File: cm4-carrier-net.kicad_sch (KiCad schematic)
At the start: 59 parts, among them J1 USB_C_Receptacle_USB2.0, J2 Micro_SD_Card, J3 Abracon_ARJM11-502, J5 block, Q1 DMP2066LSN, SW1 BOOT, SW2 GLOBAL_EN, SW3 USB_OTG, U1 TPS54302, U5 Compute_Module_4_Functional, U6 TPD2EUSB30

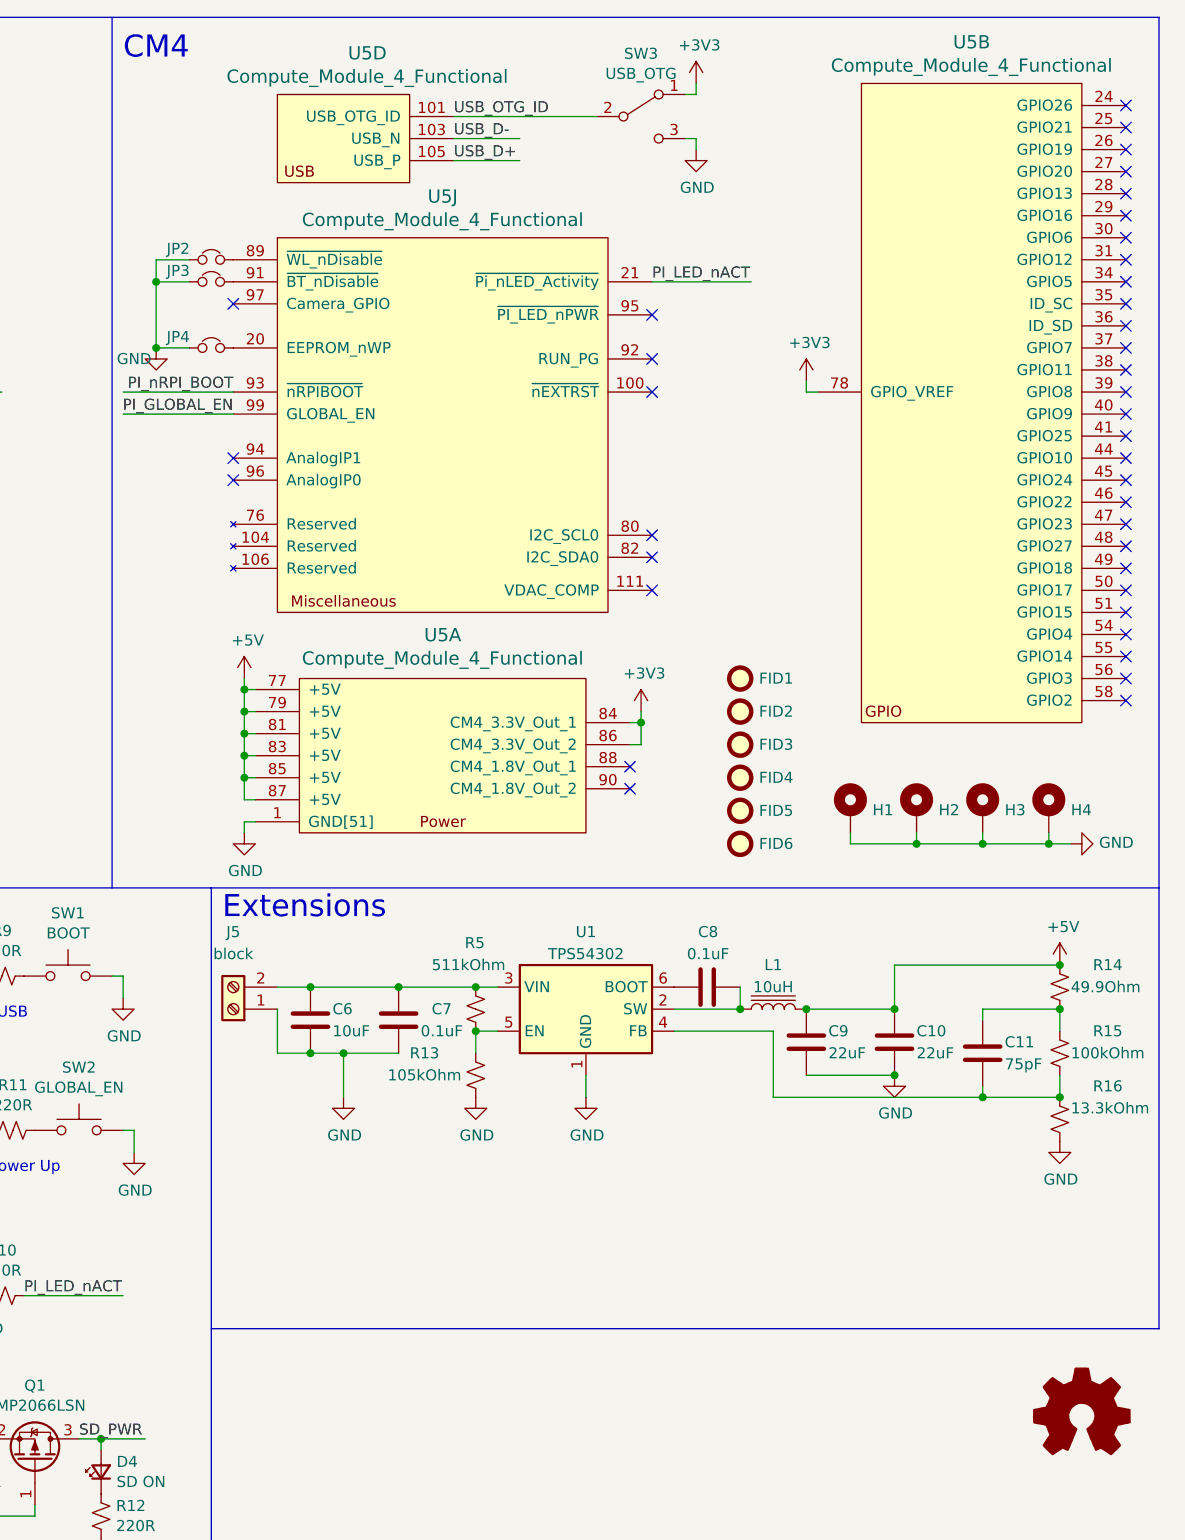
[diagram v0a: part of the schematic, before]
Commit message: added power protection and some layout changes
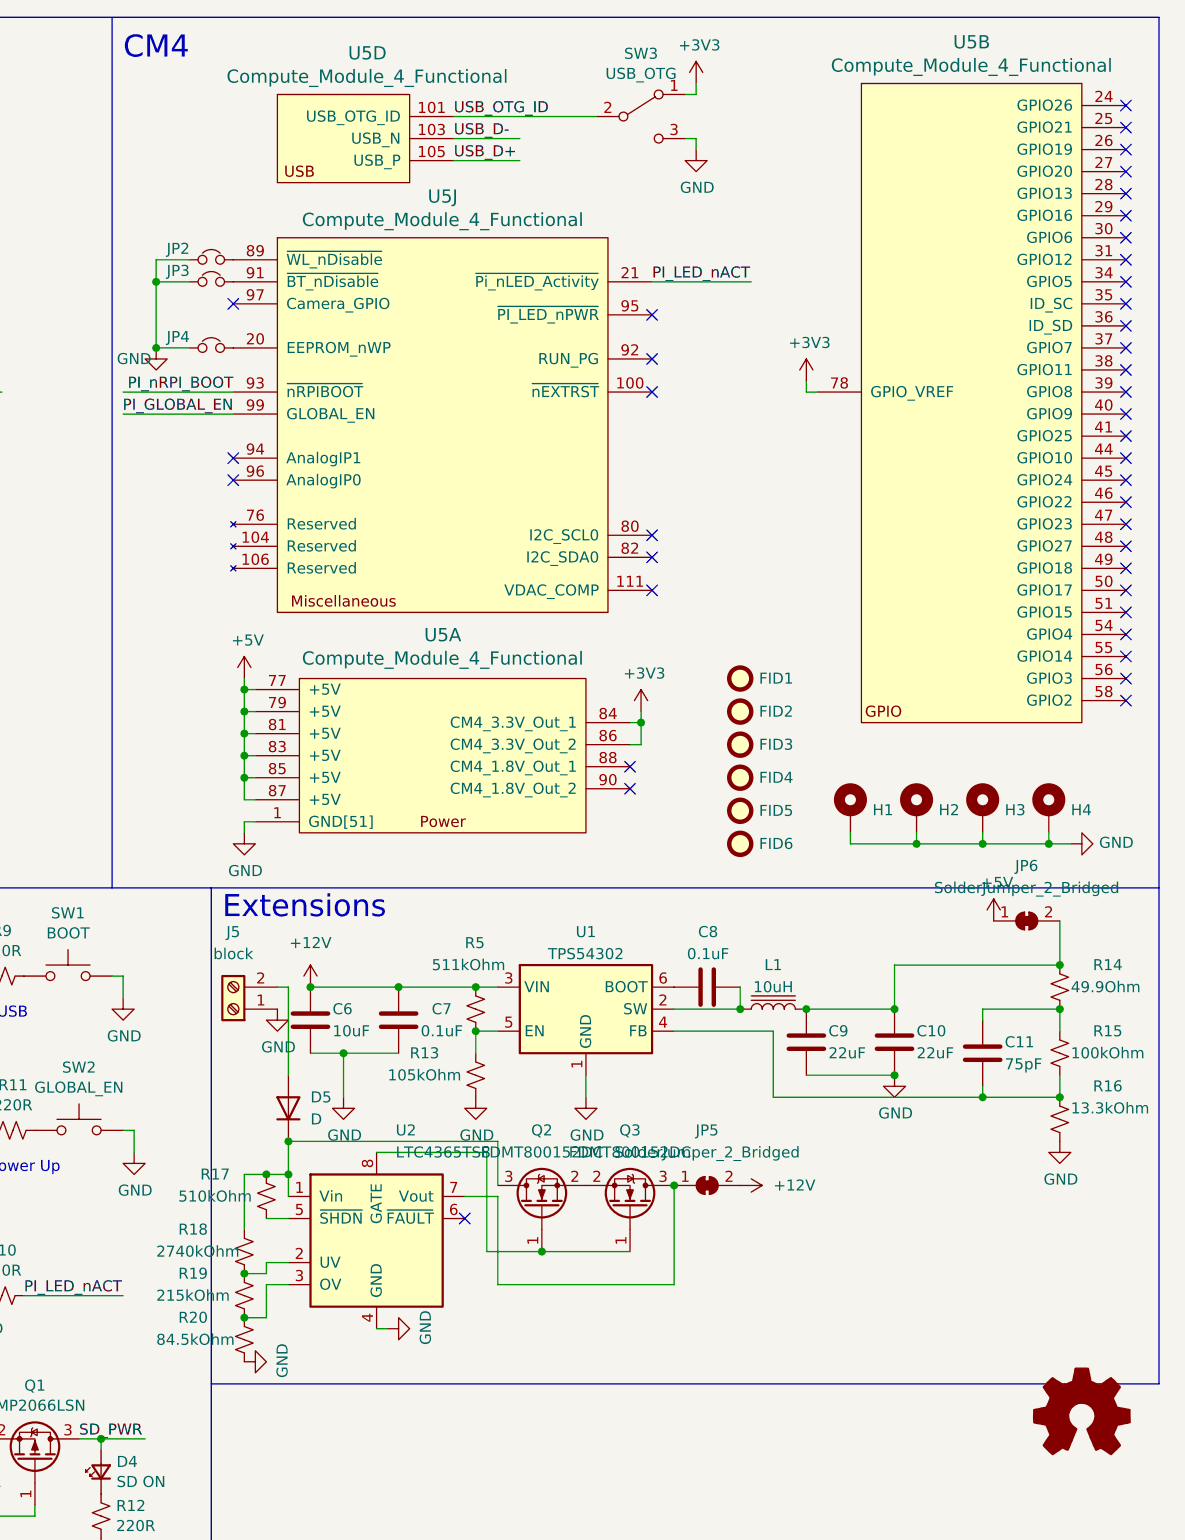
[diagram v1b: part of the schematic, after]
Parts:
- added D5: D, Diode_SMD:D_2010_5025Metric_Pad1.52x2.65mm_HandSolder, symbol Device:D
- added JP5, JP6: SolderJumper_2_Bridged, Jumper:SolderJumper-2_P1.3mm_Bridged2Bar_RoundedPad1.0x1.5mm, symbol Jumper:SolderJumper_2_Bridged
- added Q2, Q3: FDMT800152DC, Package_TO_SOT_SMD:PQFN_8x8, symbol Transistor_FET:FDMT800152DC
- added R17: 510kOhm, Resistor_SMD:R_0603_1608Metric, symbol Device:R_Small_US
- added R18: 2740kOhm, Resistor_SMD:R_0603_1608Metric, symbol Device:R_Small_US
- added R19: 215kOhm, Resistor_SMD:R_0603_1608Metric, symbol Device:R_Small_US
- added R20: 84.5kOhm, Resistor_SMD:R_0603_1608Metric, symbol Device:R_Small_US
- added U2: LTC4365TS8, Package_TO_SOT_SMD:TSOT-23-8, symbol Power_Management:LTC4365TS8
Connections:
- net +5V: now also JP6.1 (A); no longer C10.1, C9.1, L1.2, R14.1
- net GND: now also R20.2, U2.4 (GND)
- net +12V: now reaches C6.1, C7.1, R5.1, U1.3 (VIN)
- net +12V: now also JP5.2 (B); no longer J5.2 (Pin_2)
- new net: Q2.1 (G), Q3.1 (G), U2.8 (GATE)
- new net: Q2.2 (S), Q3.2 (S)
- new net: JP5.1 (A), Q3.3 (D), U2.7 (Vout)
- new net: D5.1 (K), Q2.3 (D), R17.1, R18.1, U2.1 (Vin)
- new net: R17.2, U2.5 (~{SHDN})
- new net: C10.1, C9.1, JP6.2 (B), L1.2, R14.1
- new net: R19.2, R20.1, U2.3 (OV)
- new net: D5.2 (A), J5.2 (Pin_2)
- new net: R18.2, R19.1, U2.2 (UV)
- no-connect marks 47 -> 48

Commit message: a couple of changes
fully removed cm4!
added orange pi cm4 footprint.
added extra usb 2 port.
removed unneeded diode.
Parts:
- removed D5: D, Diode_SMD:D_2010_5025Metric_Pad1.52x2.65mm_HandSolder, symbol Device:D
- removed JP1: eMMC, jkiv-library:J_Small_NC, symbol cm4-carrier-net-rescue:Jumper_NC_Small-Device
- removed JP2: ~WL_nDisable, jkiv-library:J_Small_NC, symbol cm4-carrier-net-rescue:Jumper_NC_Small-Device
- removed JP3: ~BT_nDisable, jkiv-library:J_Small_NC, symbol cm4-carrier-net-rescue:Jumper_NC_Small-Device
- removed JP4: EEPROM_nWP, jkiv-library:J_Small_NC, symbol cm4-carrier-net-rescue:Jumper_NC_Small-Device
- removed SW3: USB_OTG, Button_Switch_SMD:SW_SPDT_CK-JS102011SAQN, symbol Switch:SW_SPDT
- removed U5: Compute_Module_4_Functional, RPi_Compute_Module_4:Raspberry-Pi-4-Compute-Module, symbol cm4-carrier-net-rescue:Compute_Module_4_Functional-Raspberry_Pi_Compute_Module_4
- added J6: USB_A, Connector_USB:USB_A_Receptacle_GCT_USB1046, symbol Connector:USB_A
- added JP7: ~WL_nDisable, Jumper:SolderJumper-2_P1.3mm_Bridged2Bar_Pad1.0x1.5mm, symbol cm4-carrier-net-rescue:Jumper_NC_Small-Device
- added JP8: ~BT_nDisable, Jumper:SolderJumper-2_P1.3mm_Bridged2Bar_Pad1.0x1.5mm, symbol cm4-carrier-net-rescue:Jumper_NC_Small-Device
- added SW4: USB_OTG, Button_Switch_SMD:SW_SPDT_CK-JS102011SAQN, symbol Switch:SW_SPDT
- added U3: ORANGE_PI_CM4, Orange-Pi-CM4:MODULE_ORANGE_PI_CM4, symbol Orange-Pi-CM4:ORANGE_PI_CM4
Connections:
- net +3V3: no longer D2.2 (A), D3.2 (A), J3.13, Q1.2 (S), R8.2
- net +5V: now also C10.2, J6.1 (VBUS), U3.JP1_77 (VBUS_JP1_77), U3.JP1_79 (VBUS_JP1_79), U3.JP1_81 (VBUS_JP1_81), U3.JP1_83 (VBUS_JP1_83), U3.JP1_85 (VBUS_JP1_85), U3.JP1_87 (VBUS_JP1_87)
- net E0_LEDL: now also U3.JP1_15 (PHY0_LED2/CFG_LDO1)
- net E0_TR0+: now also U3.JP1_12 (PHY0_MDI_0+)
- net E0_TR0-: now also U3.JP1_10 (PHY0_MDI_0-)
- net E0_TR1+: now also U3.JP1_4 (PHY0_MDI_1+)
- net E0_TR1-: now also U3.JP1_6 (PHY0_MDI_1-)
- net E0_TR2+: now also U3.JP1_11 (PHY0_MDI_2+)
- net E0_TR2-: now also U3.JP1_9 (PHY0_MDI_2-)
- net E0_TR3+: now also U3.JP1_3 (PHY0_MDI_3+)
- net E0_TR3-: now also U3.JP1_5 (PHY0_MDI_3-)
- net GND: now also C10.1, J6.4 (GND), J6.5 (Shield), JP7.1, JP8.1, SW4.3 (C), U3.JP1_1 (GND_JP1_1), U3.JP1_13 (GND_JP1_13), U3.JP1_14 (GND_JP1_14), U3.JP1_2 (GND_JP1_2), U3.JP1_22 (GND_JP1_22), U3.JP1_23 (GND_JP1_23), U3.JP1_32 (GND_JP1_32), U3.JP1_33 (GND_JP1_33), U3.JP1_42 (GND_JP1_42), U3.JP1_43 (GND_JP1_43), U3.JP1_52 (GND_JP1_52), U3.JP1_53 (GND_JP1_53), U3.JP1_59 (GND_JP1_59), U3.JP1_60 (GND_JP1_60), U3.JP1_65 (GND_JP1_65), U3.JP1_66 (GND_JP1_66), U3.JP1_7 (GND_JP1_7), U3.JP1_71 (GND_JP1_71), U3.JP1_74 (GND_JP1_74), U3.JP1_8 (GND_JP1_8), U3.JP1_98 (GND_JP1_98), U3.JP2_13 (GND_JP2_13), U3.JP2_14 (GND_JP2_14), U3.JP2_19 (GND_JP2_19), U3.JP2_20 (GND_JP2_20), U3.JP2_25 (GND_JP2_25), U3.JP2_26 (GND_JP2_26), U3.JP2_31 (GND_JP2_31), U3.JP2_32 (GND_JP2_32), U3.JP2_37 (GND_JP2_37), U3.JP2_38 (GND_JP2_38), U3.JP2_44 (GND_JP2_44), U3.JP2_50 (GND_JP2_50), U3.JP2_55 (GND_JP2_55), U3.JP2_56 (GND_JP2_56), U3.JP2_61 (GND_JP2_61), U3.JP2_62 (GND_JP2_62), U3.JP2_67 (GND_JP2_67), U3.JP2_68 (GND_JP2_68), U3.JP2_7 (GND_JP2_7), U3.JP2_73 (GND_JP2_73), U3.JP2_74 (GND_JP2_74), U3.JP2_79 (GND_JP2_79), U3.JP2_8 (GND_JP2_8), U3.JP2_80 (GND_JP2_80), U3.JP2_85 (GND_JP2_85), U3.JP2_86 (GND_JP2_86), U3.JP2_91 (GND_JP2_91), U3.JP2_92 (GND_JP2_92), U3.JP2_97 (GND_JP2_97), U3.JP2_98 (GND_JP2_98), U3.JP3_1 (GND_JP3_1), U3.JP3_13 (GND_JP3_13), U3.JP3_14 (GND_JP3_14), U3.JP3_17 (GND_JP3_17), U3.JP3_2 (GND_JP3_2), U3.JP3_20 (GND_JP3_20), U3.JP3_23 (GND_JP3_23), U3.JP3_7 (GND_JP3_7); no longer C10.2
- net PI_GLOBAL_EN: now also U3.JP1_99 (PMIC_PWRON)
- net PI_LED_nACT: now also U3.JP1_21 (DIY_LED)
- net PI_nRPI_BOOT: now also U3.JP1_93 (BOOT-SW)
- net SD_CLK: now also U3.JP1_57 (SDMMC0_CLK)
- net SD_CMD: now also U3.JP1_62 (SDMMC0_CMD)
- net SD_D0: now also U3.JP1_63 (SDMMC0_D0)
- net SD_D1: now also U3.JP1_67 (SDMMC0_D1)
- net SD_D2: now also U3.JP1_69 (SDMMC0_D2)
- net SD_D3: now also U3.JP1_61 (SDMMC0_D3)
- net SD_PWR_ON: now also U3.JP1_75 (SD_PWR_ON)
- net USB_D+: now also U3.JP2_1 (USB_OTG0_ID)
- net USB_D-: now also U3.JP2_3 (USB_OTG0_DM)
- net USB_OTG_ID: now also SW4.2 (B), U3.JP2_5 (USB_OTG0_DP)
- net ~{E0_LEDL}: now also U3.JP1_17 (PHY0_LED1/CFG_LDO0)
- net ~{E0_LEDR}: now also U3.JP1_19 (PHY0_LED0/CFG_EXT)
- net at Q2.3 (D), R17.1, R18.1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: now also J5.2 (Pin_2)
- net at C9.1, JP6.2 (B), L1.2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: no longer C10.1
- new net: JP7.2, U3.JP1_89 (~{WL_DIS})
- new net: JP8.2, U3.JP1_91 (~{BT_DIS})
- new net +1V8: U3.JP1_88 (VCC_1V8_JP1_88), U3.JP1_90 (VCC_1V8_JP1_90)
- new net +3.3V: D2.2 (A), D3.2 (A), J3.13, Q1.2 (S), R8.2, SW4.1 (A), U3.JP1_78 (VCCIO6), U3.JP1_84 (VCC_3V3_JP1_84), U3.JP1_86 (VCC_3V3_JP1_86)
- new net USB+: J6.3 (D+), U3.JP3_11 (USB2_HOST2_DP)
- new net USB-: J6.2 (D-), U3.JP3_9 (USB2_HOST2_DM)
- no-connect marks 48 -> 3
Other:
- note added: "Just pretend that everything outside of the outline is in here ;)"
- note removed: "Short = use eMMC Open = use SD card"
- moved on the sheet: C10

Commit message: added a pin header for the daughter board
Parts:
- added J4: 20021121-00010C4LF, digikey-footprints:PinHeader_2x5_P1.27mm, symbol dk_Rectangular-Connectors-Headers-Male-Pins:20021121-00010C4LF
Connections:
- net +5V: now also J4.1, J4.2
- net GND: now also J4.10, J4.9
- net I2C1_SCL-: now reaches U3.JP1_80 (I2C1_SCL_M0)
- net I2C1_SCL-: now also J4.5
- net I2C1_SDA+: now reaches U3.JP1_82 (I2C1_SDA_M0)
- net I2C1_SDA+: now also J4.3
- net USB1-: now reaches U3.JP3_3 (USB2_HOST3_DM)
- net USB1-: now also J4.6
- net USB1+: now reaches U3.JP3_5 (USB2_HOST3_DP)
- net USB1+: now also J4.4
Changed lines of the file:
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@@
     (effects (font (size 1.27 1.27)) (justify left bottom))
   )
+  (label "I2C1_SDA+" (at 521.97 72.39 180) (fields_autoplaced)
+    (effects (font (size 1.27 1.27)) (justify right bottom))
+  )
   (label "E0_TR1-" (at 67.31 133.35 0) (fields_autoplaced)
     (effects (font (size 1.27 1.27)) (justify left bottom))
@@
     (effects (font (size 1.27 1.27)) (justify left bottom))
   )
+  (label "USB1+" (at 532.13 72.39 0) (fields_autoplaced)
+    (effects (font (size 1.27 1.27)) (justify left bottom))
+  )
   (label "~{E0_LEDR}" (at 26.67 123.19 180) (fields_autoplaced)
     (effects (font (size 1.27 1.27)) (justify right bottom))
@@
     (effects (font (size 1.27 1.27)) (justify right bottom))
   )
+  (label "USB1+" (at 492.76 33.02 180) (fields_autoplaced)
+    (effects (font (size 1.27 1.27)) (justify right bottom))
+  )
+  (label "USB1-" (at 532.13 74.93 0) (fields_autoplaced)
+    (effects (font (size 1.27 1.27)) (justify left bottom))
+  )
   (label "USB_D-" (at 403.86 12.7 180) (fields_autoplaced)
     (effects (font (size 1.27 1.27)) (justify right bottom))
   )
+  (label "I2C1_SCL-" (at 386.08 127 0) (fields_autoplaced)
+    (effects (font (size 1.27 1.27)) (justify left bottom))
+  )
   (label "E0_TR0-" (at 386.08 38.1 0) (fields_autoplaced)
     (effects (font (size 1.27 1.27)) (justify left bottom))
@@
     (effects (font (size 1.27 1.27)) (justify right bottom))
   )
+  (label "I2C1_SCL-" (at 521.97 74.93 180) (fields_autoplaced)
+    (effects (font (size 1.27 1.27)) (justify right bottom))
+  )
   (label "E0_TR2-" (at 67.31 125.73 0) (fields_autoplaced)
     (effects (font (size 1.27 1.27)) (justify left bottom))
@@
     (effects (font (size 1.27 1.27)) (justify right bottom))
   )
+  (label "I2C1_SDA+" (at 386.08 129.54 0) (fields_autoplaced)
+    (effects (font (size 1.27 1.27)) (justify left bottom))
+  )
   (label "E0_TR0+" (at 67.31 140.97 0) (fields_autoplaced)
     (effects (font (size 1.27 1.27)) (justify left bottom))
@@
     (effects (font (size 1.27 1.27)) (justify right bottom))
   )
+  (label "USB1-" (at 492.76 30.48 180) (fields_autoplaced)
+    (effects (font (size 1.27 1.27)) (justify right bottom))
+  )
   (label "SD_D3" (at 309.88 104.14 180) (fields_autoplaced)
     (effects (font (size 1.27 1.27)) (justify right bottom))
@@
     )
   )
+  (symbol (lib_id "power:GND") (at 521.97 80.01 270) (unit 1)
+    (in_bom yes) (on_board yes) (dnp no) (fields_autoplaced)
+    (property "Reference" "#PWR023" (at 515.62 80.01 0)
+      (effects (font (size 1.27 1.27)) hide)
+    )
+    (property "Value" "GND" (at 518.16 80.01 90)
+      (effects (font (size 1.27 1.27)) (justify right))
+    )
+    (property "Footprint" "" (at 521.97 80.01 0)
+      (effects (font (size 1.27 1.27)) hide)
+    )
+    (property "Datasheet" "" (at 521.97 80.01 0)
+      (effects (font (size 1.27 1.27)) hide)
+    )
+    (pin "1")
+    (instances
+      (project "cm4-carrier-net"
+        (path "/a58a5c23-cf42-4abb-bf4c-19a657300252"
+          (reference "#PWR023") (unit 1)
+        )
+      )
+    )
+  )
   (symbol (lib_id "power:GND") (at 257.81 116.84 270) (unit 1)
     (in_bom yes) (on_board yes) (dnp no)
@@
   )
   (symbol (lib_id "power:+3.3V") (at 389.89 132.08 0) (unit 1)
-    (in_bom yes) (on_board yes) (dnp no) (fields_autoplaced)
+    (in_bom yes) (on_board yes) (dnp no)
     (property "Reference" "#PWR025" (at 389.89 135.89 0)
       (effects (font (size 1.27 1.27)) hide)
     )
-    (property "Value" "+3.3V" (at 389.89 127 0)
+    (property "Value" "+3.3V" (at 393.7 132.08 0)
       (effects (font (size 1.27 1.27)))
     )
@@
     )
   )
+  (symbol (lib_id "power:+5V") (at 521.97 69.85 90) (unit 1)
+    (in_bom yes) (on_board yes) (dnp no)
+    (property "Reference" "#PWR022" (at 525.78 69.85 0)
+      (effects (font (size 1.27 1.27)) hide)
+    )
+    (property "Value" "+5V" (at 518.16 68.58 0)
+      (effects (font (size 1.27 1.27)))
+    )
+    (property "Footprint" "" (at 521.97 69.85 0)
+      (effects (font (size 1.27 1.27)) hide)
+    )
+    (property "Datasheet" "" (at 521.97 69.85 0)
+      (effects (font (size 1.27 1.27)) hide)
+    )
+    (pin "1")
+    (instances
+      (project "cm4-carrier-net"
+        (path "/a58a5c23-cf42-4abb-bf4c-19a657300252"
+          (reference "#PWR022") (unit 1)
+        )
+      )
+    )
+  )
   (symbol (lib_id "power:GND") (at 495.3 85.09 0) (unit 1)
     (in_bom yes) (on_board yes) (dnp no) (fields_autoplaced)
@@
   )
   (symbol (lib_id "power:+1V8") (at 389.89 137.16 0) (unit 1)
-    (in_bom yes) (on_board yes) (dnp no) (fields_autoplaced)
+    (in_bom yes) (on_board yes) (dnp no)
     (property "Reference" "#PWR026" (at 389.89 140.97 0)
       (effects (font (size 1.27 1.27)) hide)
     )
-    (property "Value" "+1V8" (at 389.89 132.08 0)
+    (property "Value" "+1V8" (at 393.7 137.16 0)
       (effects (font (size 1.27 1.27)))
     )
@@
     )
   )
+  (symbol (lib_id "dk_Rectangular-Connectors-Headers-Male-Pins:20021121-00010C4LF") (at 527.05 74.93 0) (unit 1)
+    (in_bom yes) (on_board yes) (dnp no) (fields_autoplaced)
+    (property "Reference" "J4" (at 527.05 63.5 0)
+      (effects (font (size 1.27 1.27)))
+    )
+    (property "Value" "20021121-00010C4LF" (at 527.05 66.04 0)
+      (effects (font (size 1.27 1.27)))
+    )
+    (property "Footprint" "digikey-footprints:PinHeader_2x5_P1.27mm" (at 532.13 69.85 0)
+      (effects (font (size 1.524 1.524)) (justify left) hide)
+    )
+    (property "Datasheet" "https://cdn.amphenol-icc.com/media/wysiwyg/files/drawing/20021121.pdf" (at 532.13 67.31 0)
+      (effects (font (size 1.524 1.524)) (justify left) hide)
+    )
+    (property "Digi-Key_PN" "609-3695-1-ND" (at 532.13 64.77 0)
+      (effects (font (size 1.524 1.524)) (justify left) hide)
+    )
+    (property "MPN" "20021121-00010C4LF" (at 532.13 62.23 0)
+      (effects (font (size 1.524 1.524)) (justify left) hide)
+    )
+    (property "Category" "Connectors, Interconnects" (at 532.13 59.69 0)
+      (effects (font (size 1.524 1.524)) (justify left) hide)
+    )
+    (property "Family" "Rectangular Connectors - Headers, Male Pins" (at 532.13 57.15 0)
+      (effects (font (size 1.524 1.524)) (justify left) hide)
+    )
+    (property "DK_Datasheet_Link" "https://cdn.amphenol-icc.com/media/wysiwyg/files/drawing/20021121.pdf" (at 532.13 54.61 0)
+      (effects (font (size 1.524 1.524)) (justify left) hide)
+    )
+    (property "DK_Detail_Page" "/product-detail/en/amphenol-icc-fci/20021121-00010C4LF/609-3695-1-ND/2209147" (at 532.13 52.07 0)
+      (effects (font (size 1.524 1.524)) (justify left) hide)
+    )
+    (property "Description" "CONN HEADER SMD 10POS 1.27MM" (at 532.13 49.53 0)
+      (effects (font (size 1.524 1.524)) (justify left) hide)
+    )
+    (property "Manufacturer" "Amphenol ICC (FCI)" (at 532.13 46.99 0)
+      (effects (font (size 1.524 1.524)) (justify left) hide)
+    )
+    (property "Status" "Active" (at 532.13 44.45 0)
+      (effects (font (size 1.524 1.524)) (justify left) hide)
+    )
+    (pin "3")
+    (pin "5")
+    (pin "7")
+    (pin "9")
+    (pin "10")
+    (pin "1")
+    (pin "6")
+    (pin "4")
+    (pin "8")
+    (pin "2")
+    (instances
+      (project "cm4-carrier-net"
+        (path "/a58a5c23-cf42-4abb-bf4c-19a657300252"
+          (reference "J4") (unit 1)
+        )
+      )
+    )
+  )
   (symbol (lib_id "Device:R_Small_US") (at 205.74 134.62 0) (unit 1)
     (in_bom yes) (on_board yes) (dnp no)
@@
         )
       )
+    )
+  )
+  (symbol (lib_id "power:+5V") (at 532.13 69.85 270) (unit 1)
+    (in_bom yes) (on_board yes) (dnp no)
+    (property "Reference" "#PWR024" (at 528.32 69.85 0)
+      (effects (font (size 1.27 1.27)) hide)
+    )
+    (property "Value" "+5V" (at 535.94 68.58 0)
+      (effects (font (size 1.27 1.27)))
+    )
+    (property "Footprint" "" (at 532.13 69.85 0)
+      (effects (font (size 1.27 1.27)) hide)
+    )
+    (property "Datasheet" "" (at 532.13 69.85 0)
+      (effects (font (size 1.27 1.27)) hide)
+    )
+    (pin "1")
+    (instances
+      (project "cm4-carrier-net"
+        (path "/a58a5c23-cf42-4abb-bf4c-19a657300252"
+          (reference "#PWR024") (unit 1)
+        )
+      )
+    )
+  )
+  (symbol (lib_id "power:GND") (at 532.13 80.01 90) (unit 1)
+    (in_bom yes) (on_board yes) (dnp no) (fields_autoplaced)
+    (property "Reference" "#PWR030" (at 538.48 80.01 0)
+      (effects (font (size 1.27 1.27)) hide)
+    )
+    (property "Value" "GND" (at 535.94 80.01 90)
+      (effects (font (size 1.27 1.27)) (justify right))
+    )
+    (property "Footprint" "" (at 532.13 80.01 0)
+      (effects (font (size 1.27 1.27)) hide)
+    )
+    (property "Datasheet" "" (at 532.13 80.01 0)
+      (effects (font (size 1.27 1.27)) hide)
+    )
+    (pin "1")
+    (instances
+      (project "cm4-carrier-net"
+        (path "/a58a5c23-cf42-4abb-bf4c-19a657300252"
+          (reference "#PWR030") (unit 1)
+        )
+      )
